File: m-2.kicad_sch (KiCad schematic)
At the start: 23 parts, among them J1 Bus_M.2_1-2199230-6, M3 Mech_M2_2280_H2.5mm

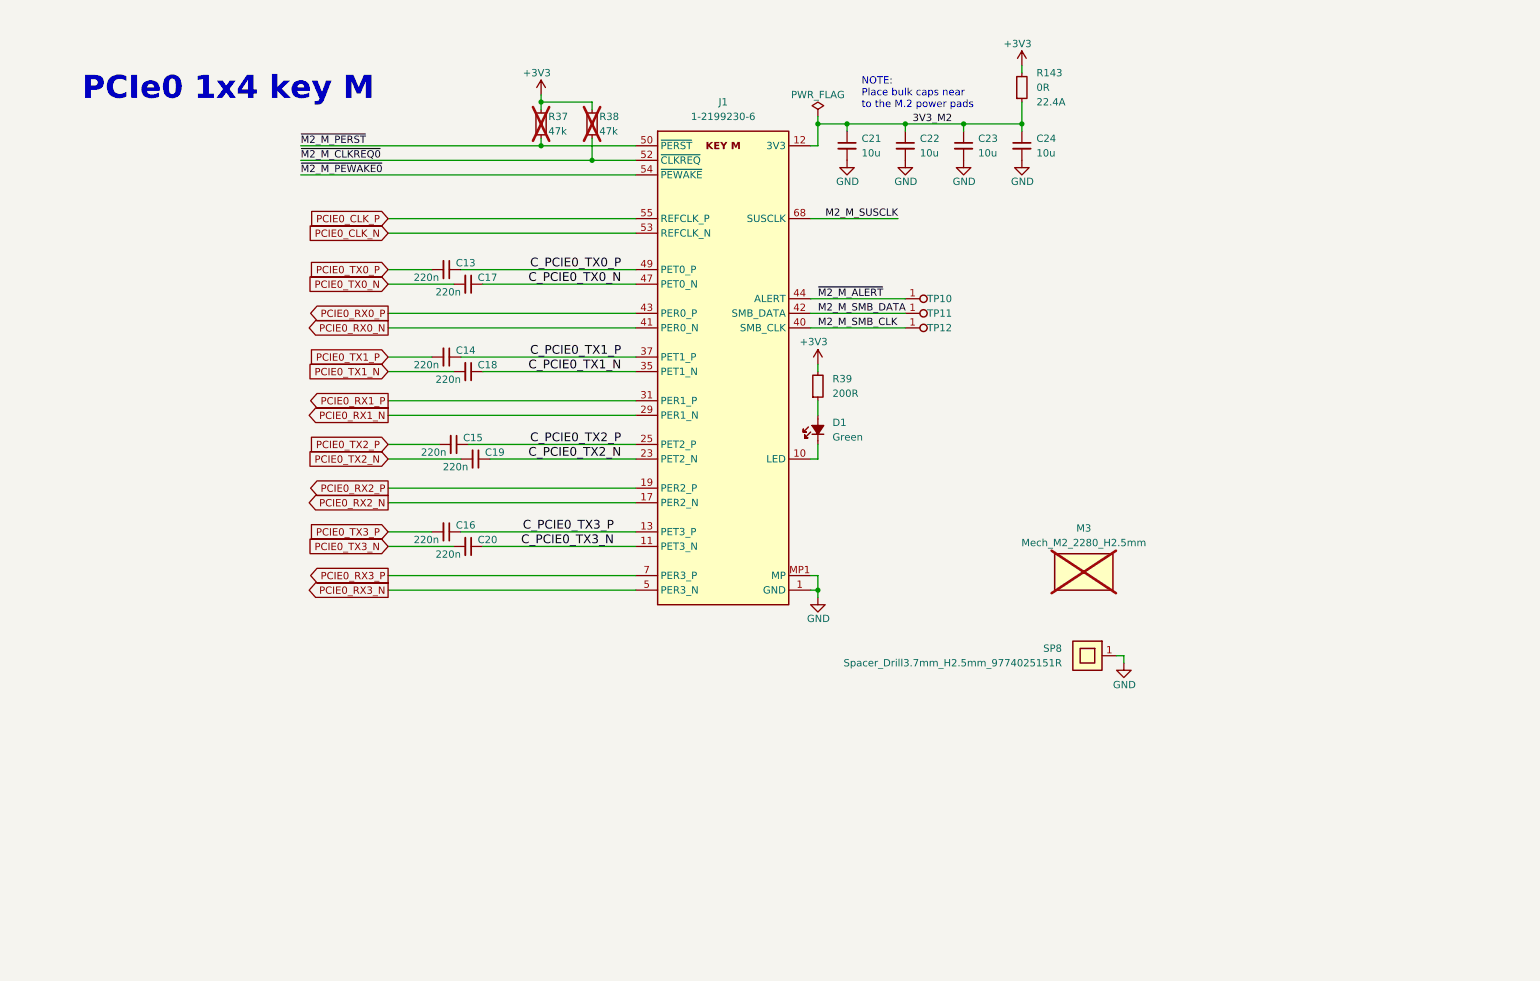
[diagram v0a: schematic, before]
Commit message: [#100765] Update M.2 subsheet
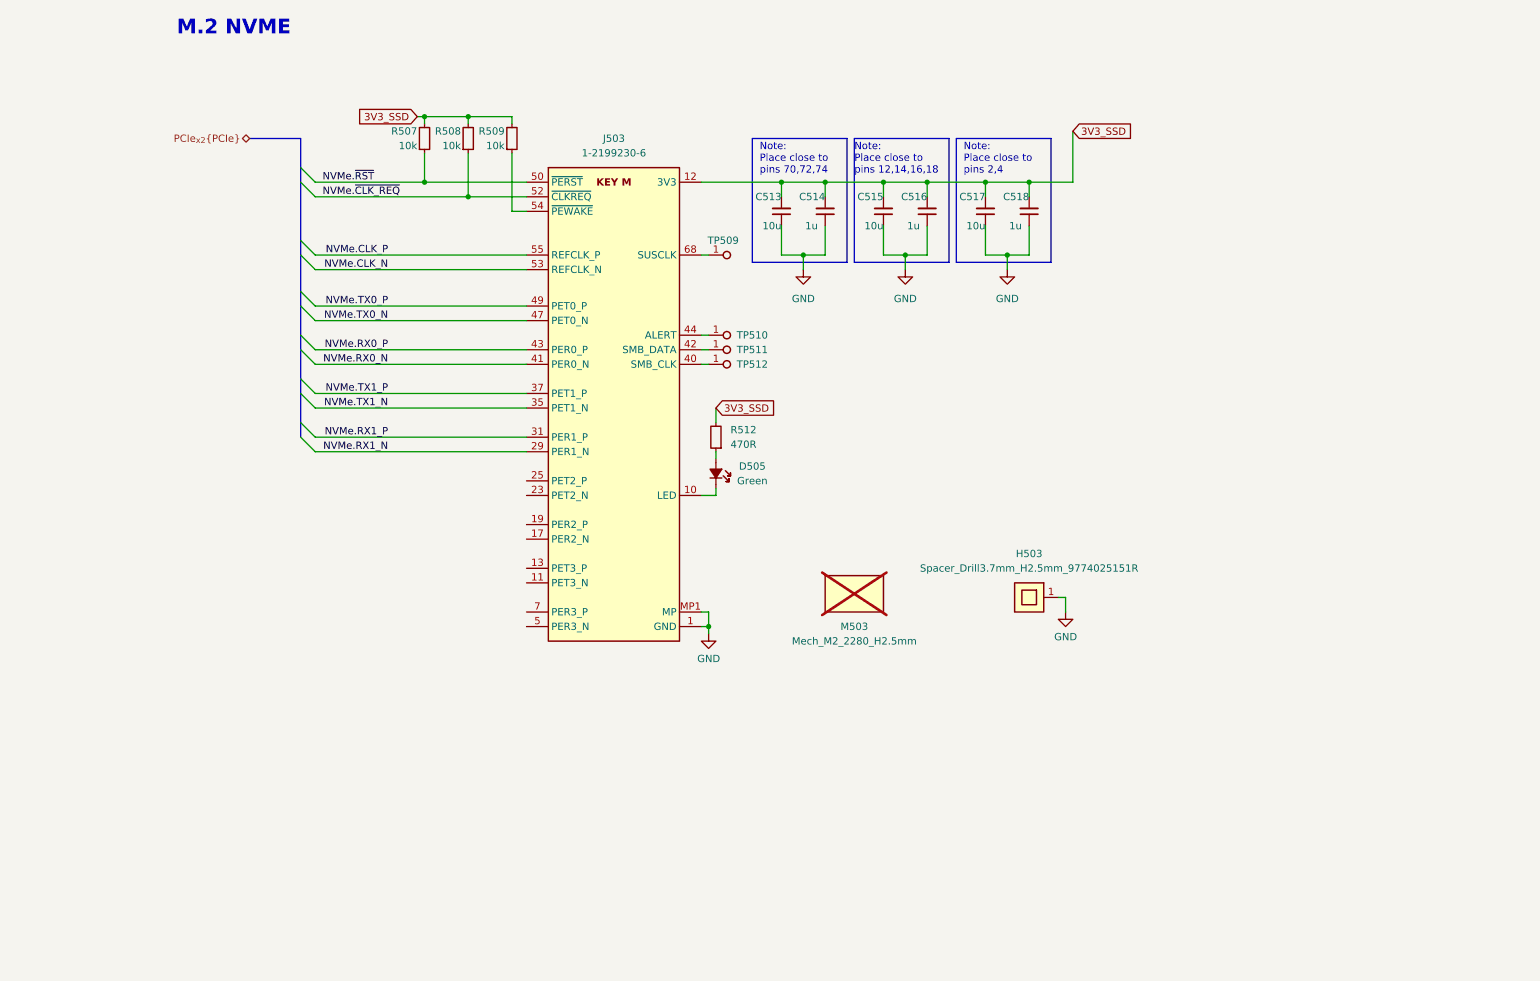
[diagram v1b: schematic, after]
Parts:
- removed C13, C14, C15, C16, C17, C18, C19, C20: C_220n_0402, jetson-orin-baseboard-footprints:C_0402_1005Metric, symbol jetson-orin-baseboard:C_220n_0402
- removed C21, C22, C23, C24: C_10u_0603, jetson-orin-baseboard-footprints:C_0603_1608Metric, symbol jetson-orin-baseboard:C_10u_0603
- removed D1: LED_G_0603_LTST-C190GKT, jetson-orin-baseboard-footprints:LED_0603_1608Metric_G, symbol jetson-orin-baseboard:LED_G_0603_LTST-C190GKT
- removed J1: Bus_M.2_1-2199230-6, antmicro-footprints:Bus_M.2_Socket_Key_M_TE_1-2199230-6, symbol antmicroPciConnectors:Bus_M.2_1-2199230-6
- removed M3: Mech_M2_2280_H2.5mm, jetson-orin-baseboard-footprints:Mech_M2_2280_H2.5mm, symbol jetson-orin-baseboard:Mech_M2_2280_H2.5mm
- removed R143: R_0R_22.4A_0603, jetson-orin-baseboard-footprints:R_0603_1608Metric, symbol jetson-orin-baseboard:R_0R_22.4A_0603
- removed R37, R38: R_47k_0402, jetson-orin-baseboard-footprints:R_0402_1005Metric, symbol jetson-orin-baseboard:R_47k_0402
- removed R39: R_200R_0402, jetson-orin-baseboard-footprints:R_0402_1005Metric, symbol jetson-orin-baseboard:R_200R_0402
- removed SP8: Spacer_Drill3.7mm_H2.5mm_9774025151R, jetson-orin-baseboard-footprints:Spacer_Drill3.7mm_H2.5mm_9774025151R, symbol jetson-orin-baseboard:Spacer_Drill3.7mm_H2.5mm_9774025151R
- removed TP10, TP11, TP12: TP_0.75mm_SMD, jetson-orin-baseboard-footprints:TP_SMD_0.75mm, symbol jetson-orin-baseboard:TP_0.75mm_SMD
- added C513, C515, C517: C_10u_0402, antmicro-footprints:C_0402_1005Metric, symbol antmicroCapacitors0402:C_10u_0402
- added C514, C516, C518: C_1u_0402, antmicro-footprints:C_0402_1005Metric, symbol antmicroCapacitors0402:C_1u_0402
- added D505: LED_G_0603_KP-1608CGCK, antmicro-footprints:LED_0603_1608Metric_G, symbol antmicroLEDIndicationDiscrete:LED_G_0603_KP-1608CGCK
- added H503: Spacer_Drill3.7mm_H2.5mm_9774025151R, antmicro-footprints:Spacer_Drill3.7mm_H2.5mm_9774025151R, symbol antmicroMechanicalParts:Spacer_Drill3.7mm_H2.5mm_9774025151R
- added J503: Bus_M.2_1-2199230-6, antmicro-footprints:Bus_M.2_Socket_Key_M_TE_1-2199230-6, symbol antmicroPciConnectors:Bus_M.2_1-2199230-6
- added M503: Mech_M2_2280_H2.5mm, antmicro-footprints:Mech_M2_2280_H2.5mm, symbol antmicroModules:Mech_M2_2280_H2.5mm
- added R507, R508, R509: R_10k_0402, antmicro-footprints:R_0402_1005Metric, symbol antmicroResistors0402:R_10k_0402
- added R512: R_470R_0402, antmicro-footprints:R_0402_1005Metric, symbol antmicroResistors0402:R_470R_0402
- added TP509, TP510, TP511, TP512: TP_0.75mm_SMD, antmicro-footprints:TP_SMD_0.75mm, symbol antmicroTestPoints:TP_0.75mm_SMD
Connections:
- net GND: now also C513.1, C514.1, C515.1, C516.1, C517.1, C518.1, H503.1, J503.1 (GND), J503.15 (GND), J503.21 (GND), J503.27 (GND), J503.3 (GND), J503.33 (GND), J503.39 (GND), J503.45 (GND), J503.51 (GND), J503.57 (GND), J503.71 (GND), J503.73 (GND), J503.75 (GND), J503.9 (GND), J503.MP1 (MP), J503.MP2 (MP)
- new net: J503.40 (SMB_CLK), TP512.1
- new net: D505.2 (A), R512.1
- new net: J503.54 (~{PEWAKE}), R509.1
- new net: D505.1 (C), J503.10 (LED)
- new net: J503.42 (SMB_DATA), TP511.1
- new net: J503.44 (ALERT), TP510.1
- new net: J503.68 (SUSCLK), TP509.1
- new net 3V3_SSD: C513.2, C514.2, C515.2, C516.2, C517.2, C518.2, J503.12 (3V3), J503.14 (3V3), J503.16 (3V3), J503.18 (3V3), J503.2 (3V3), J503.4 (3V3), J503.70 (3V3), J503.72 (3V3), J503.74 (3V3), R507.2, R508.2, R509.2, R512.2
- new net NVMe.CLK_N: J503.53 (REFCLK_N)
- new net NVMe.CLK_P: J503.55 (REFCLK_P)
- new net NVMe.RX0_N: J503.41 (PER0_N)
- new net NVMe.RX0_P: J503.43 (PER0_P)
- new net NVMe.RX1_N: J503.29 (PER1_N)
- new net NVMe.RX1_P: J503.31 (PER1_P)
- new net NVMe.TX0_N: J503.47 (PET0_N)
- new net NVMe.TX0_P: J503.49 (PET0_P)
- new net NVMe.TX1_N: J503.35 (PET1_N)
- new net NVMe.TX1_P: J503.37 (PET1_P)
- new net NVMe.~{CLK_REQ}: J503.52 (~{CLKREQ}), R508.1
- new net NVMe.~{RST}: J503.50 (~{PERST}), R507.1
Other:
- note added: "M.2 NVME"
- note added: "Note: Place close to pins 12,14,16,18"
- note added: "Note: Place close to pins 2,4"
- note added: "Note: Place close to pins 70,72,74"
- note removed: "NOTE: Place bulk caps near to the M.2 power pads"
- note removed: "PCIe0 1x4 key M"

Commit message: [#100765] Update subsheets
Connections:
- net NVMe.CLK_N renamed PCIe_{x2}.CLK_N
- net NVMe.CLK_P renamed PCIe_{x2}.CLK_P
- net NVMe.RX0_N renamed PCIe_{x2}.RX0_N
- net NVMe.RX0_P renamed PCIe_{x2}.RX0_P
- net NVMe.RX1_N renamed PCIe_{x2}.RX1_N
- net NVMe.RX1_P renamed PCIe_{x2}.RX1_P
- net NVMe.TX0_N renamed PCIe_{x2}.TX0_N
- net NVMe.TX0_P renamed PCIe_{x2}.TX0_P
- net NVMe.TX1_N renamed PCIe_{x2}.TX1_N
- net NVMe.TX1_P renamed PCIe_{x2}.TX1_P
- net NVMe.~{CLK_REQ} renamed PCIe_{x2}.~{CLK_REQ}
- net NVMe.~{RST} renamed PCIe_{x2}.~{RST}
- no-connect marks 0 -> 8

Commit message: [#100765] Update schematic
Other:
- note added: "TODO: add 0R on PCIe RX/TX lines (?)"
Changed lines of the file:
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@@
+		)
+	)
+	(text "TODO: add 0R on PCIe RX/TX lines (?)"
+		(exclude_from_sim no)
+		(at 68.58 76.708 0)
+		(effects
+			(font
+				(size 1.27 1.27)
+			)
 		)
 	)

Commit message: [#100765] Update M.2 3V3 line
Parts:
- added R30: R_0R_22.4A_0603, antmicro-footprints:R_0603_1608Metric, symbol antmicroResistors0603:R_0R_22.4A_0603
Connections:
- net 3V3_SSD: no longer names the net of C513.2, C514.2, C515.2, C516.2, C517.2, C518.2, J503.12 (3V3), J503.14 (3V3), J503.16 (3V3), J503.18 (3V3), J503.2 (3V3), J503.4 (3V3), J503.70 (3V3), J503.72 (3V3), J503.74 (3V3)
- net 3V3_SSD: now also R30.1; no longer R507.2, R508.2, R509.2, R512.2
- new net +3V3: R30.2, R507.2, R508.2, R509.2, R512.2

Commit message: [#100765] Update schematic
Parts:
- added R70: R_0R_0402, antmicro-footprints:R_0402_1005Metric, symbol antmicroResistors0402:R_0R_0402
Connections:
- net PCIe_{x2}.~{RST}: now also R70.2; no longer J503.50 (~{PERST}), R507.1
- new net: J503.50 (~{PERST}), R507.1, R70.1

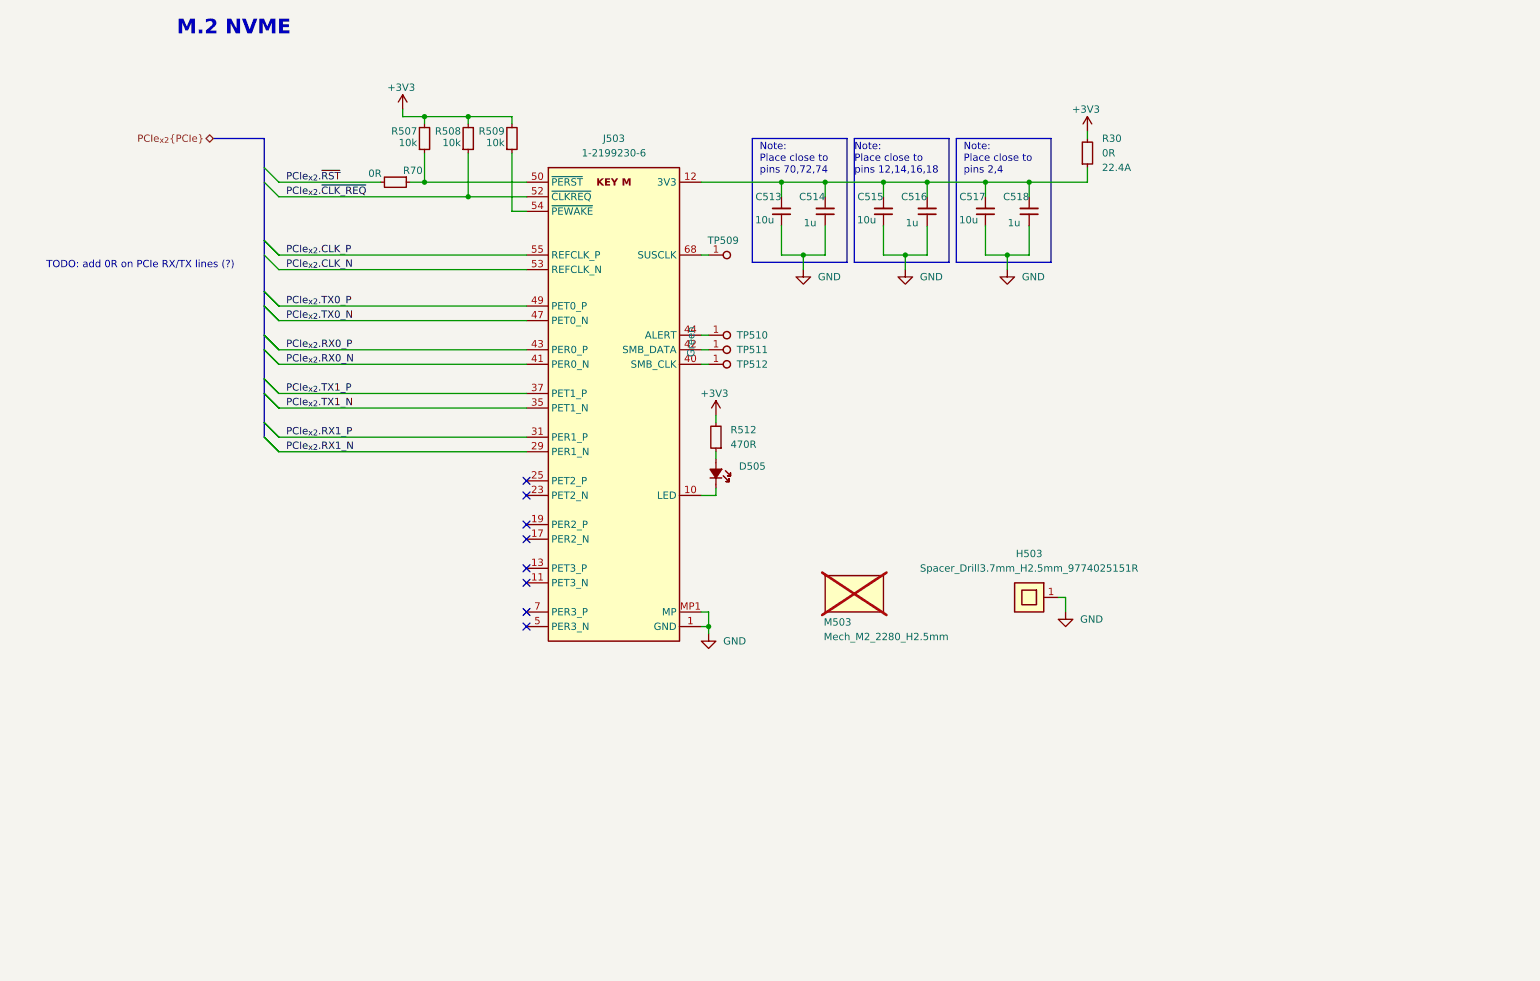
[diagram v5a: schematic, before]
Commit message: [#100765] Change sheet format to A3, update schematic
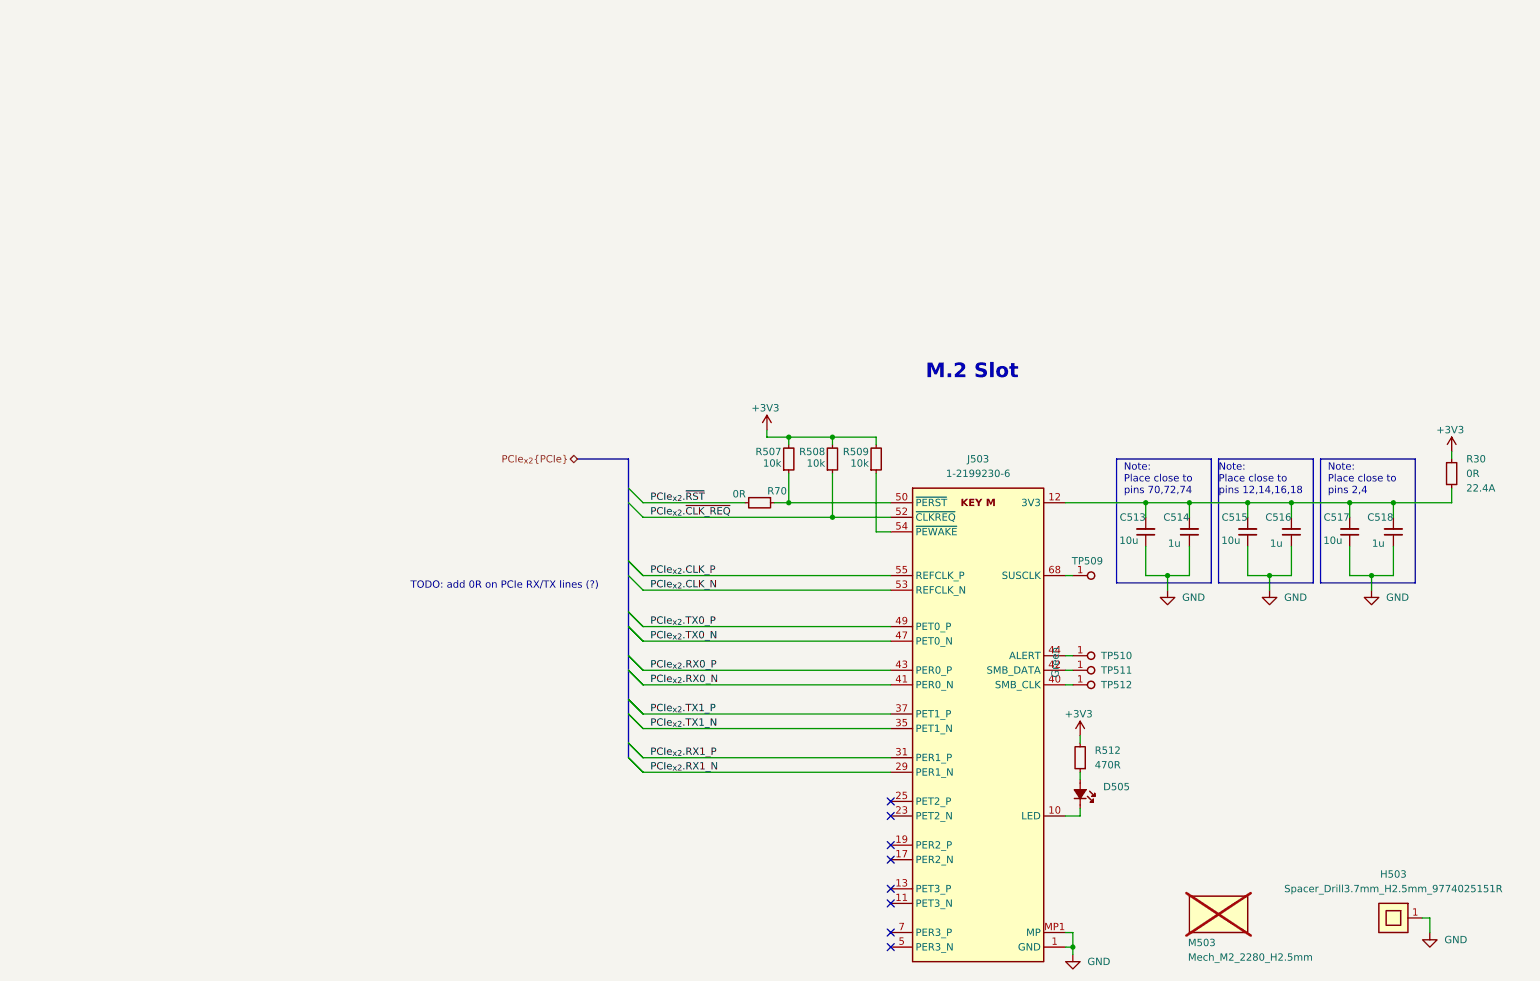
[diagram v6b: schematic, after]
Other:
- note added: "M.2 Slot"
- note removed: "M.2 NVME"
- company: (none) -> Antmicro
- title: (none) -> antmicro-jetson-orin-baseboard-pcie-switch-expansion-hw
- moved on the sheet: C513, C514, C515, C516, C517, C518, D505, H503, J503, M503, R30, R507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

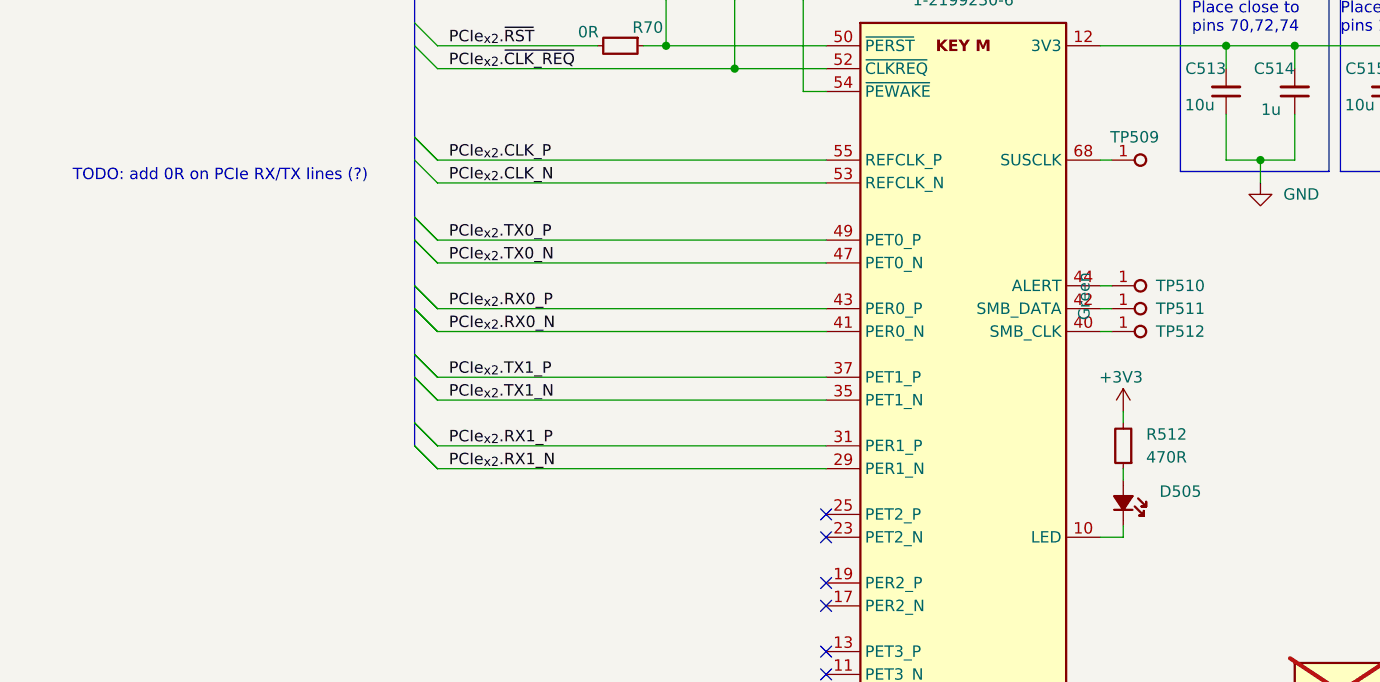
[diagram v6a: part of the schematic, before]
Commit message: [#100765] WIP: Apply review changes
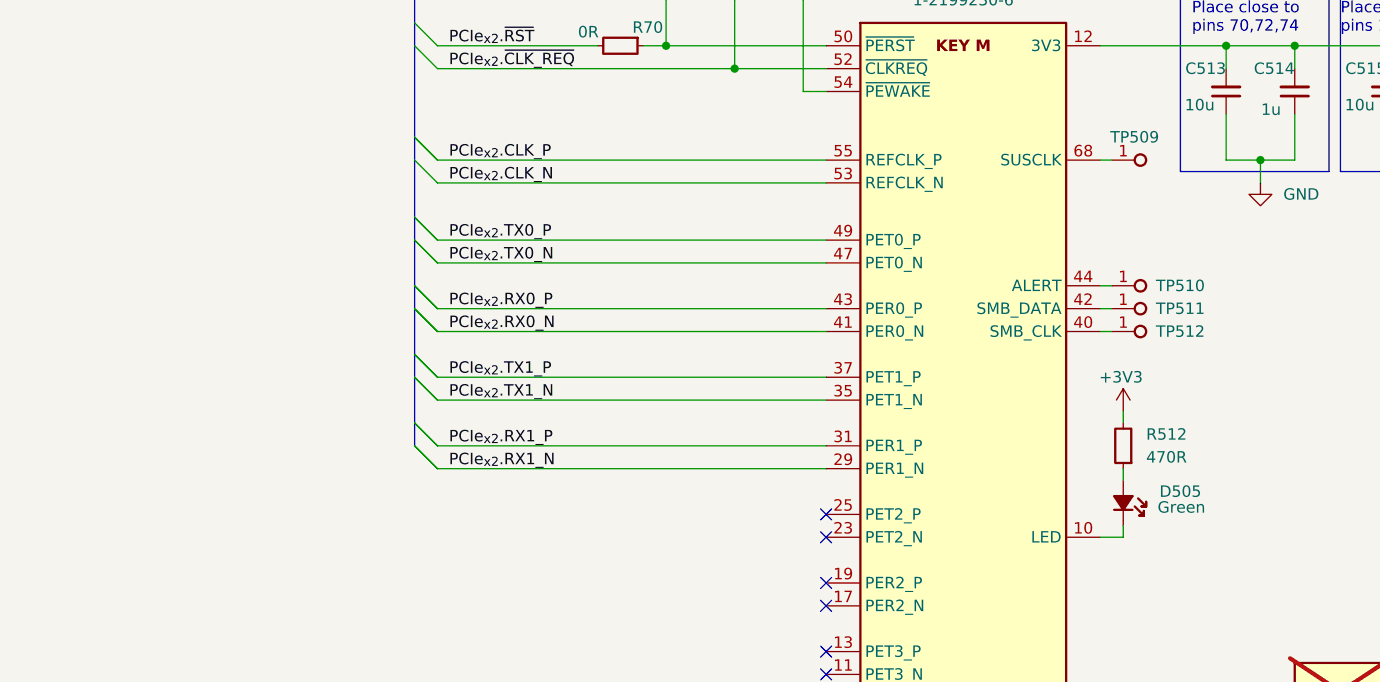
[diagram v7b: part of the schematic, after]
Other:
- note removed: "TODO: add 0R on PCIe RX/TX lines (?)"
